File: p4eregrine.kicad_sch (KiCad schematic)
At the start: 45 parts, among them U1 ESP32-P4NRW32X, U15 TPD2EUSB30A, U3 W25Q128JVP, Y1 Crystal_GND24

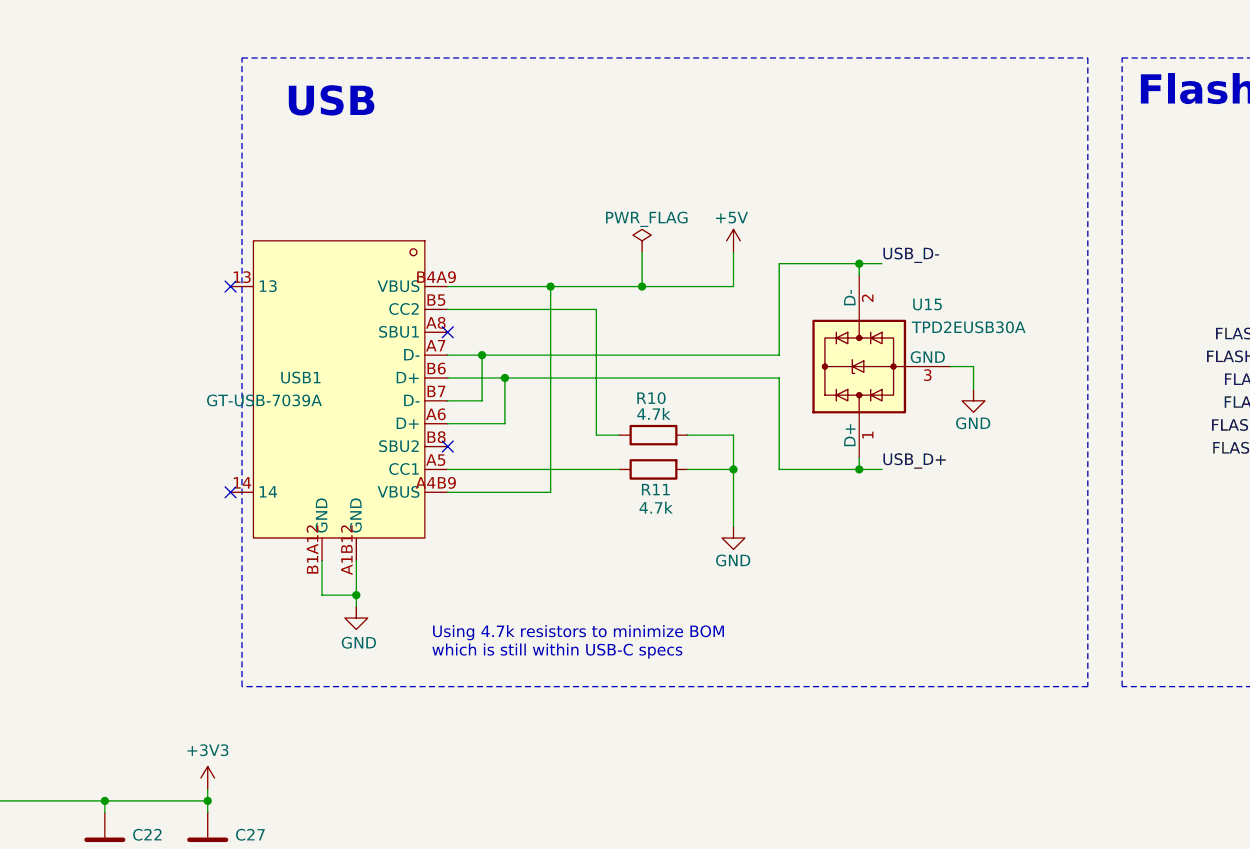
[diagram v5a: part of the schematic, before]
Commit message: Fix some silkscreen overlapping copper issues
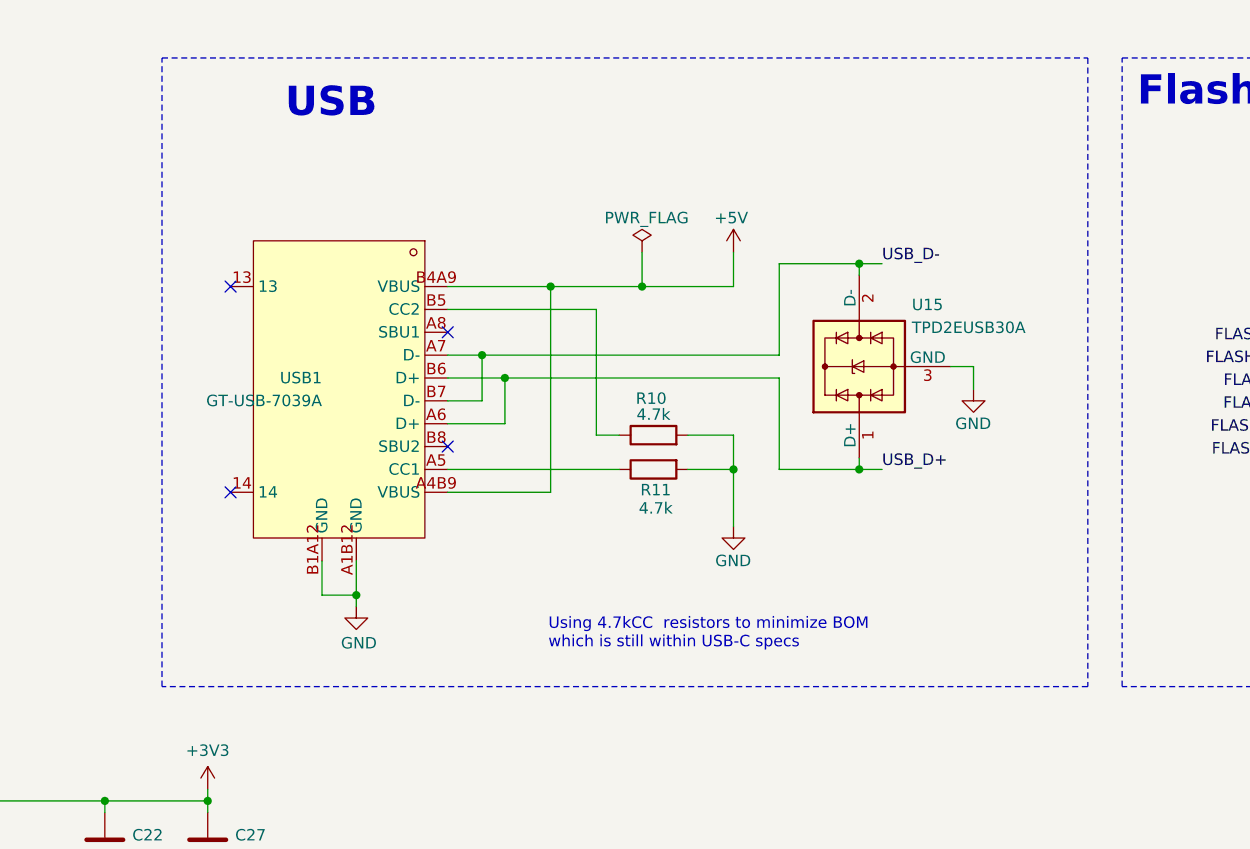
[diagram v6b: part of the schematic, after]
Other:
- note added: "Using 4.7kCC resistors to minimize BOM which is still within USB-C specs"
- note removed: "Using 4.7k resistors to minimize BOM which is still within USB-C specs"
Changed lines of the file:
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@@
 	)
 	(rectangle
-		(start 240.03 19.05)
+		(start 231.14 19.05)
 		(end 334.01 88.9)
 		(stroke
@@
 		)
 	)
-	(text "Using 4.7k resistors to minimize BOM\nwhich is still within USB-C specs"
+	(text "Using 4.7kCC  resistors to minimize BOM\nwhich is still within USB-C specs"
 		(exclude_from_sim no)
-		(at 261.112 84.074 0)
+		(at 274.066 83.058 0)
 		(effects
 			(font

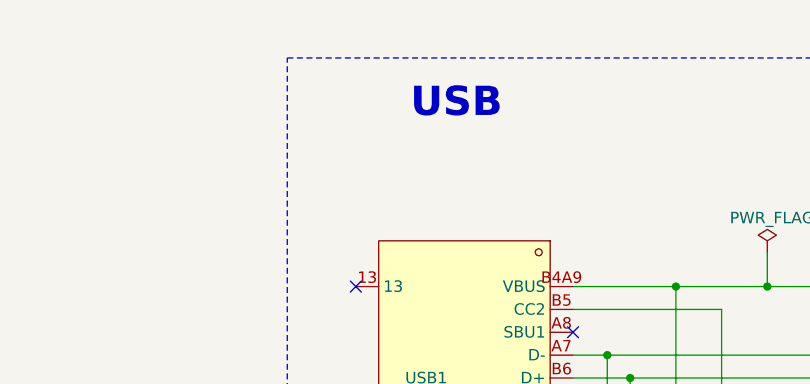
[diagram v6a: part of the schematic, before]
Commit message: Make GND probe pads square
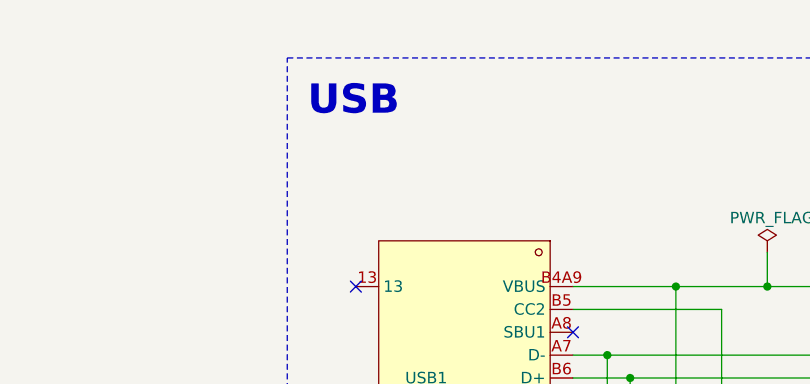
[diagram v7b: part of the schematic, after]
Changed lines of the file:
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@@
 	(text "USB"
 		(exclude_from_sim no)
-		(at 249.936 24.13 0)
+		(at 238.506 23.876 0)
 		(effects
 			(font

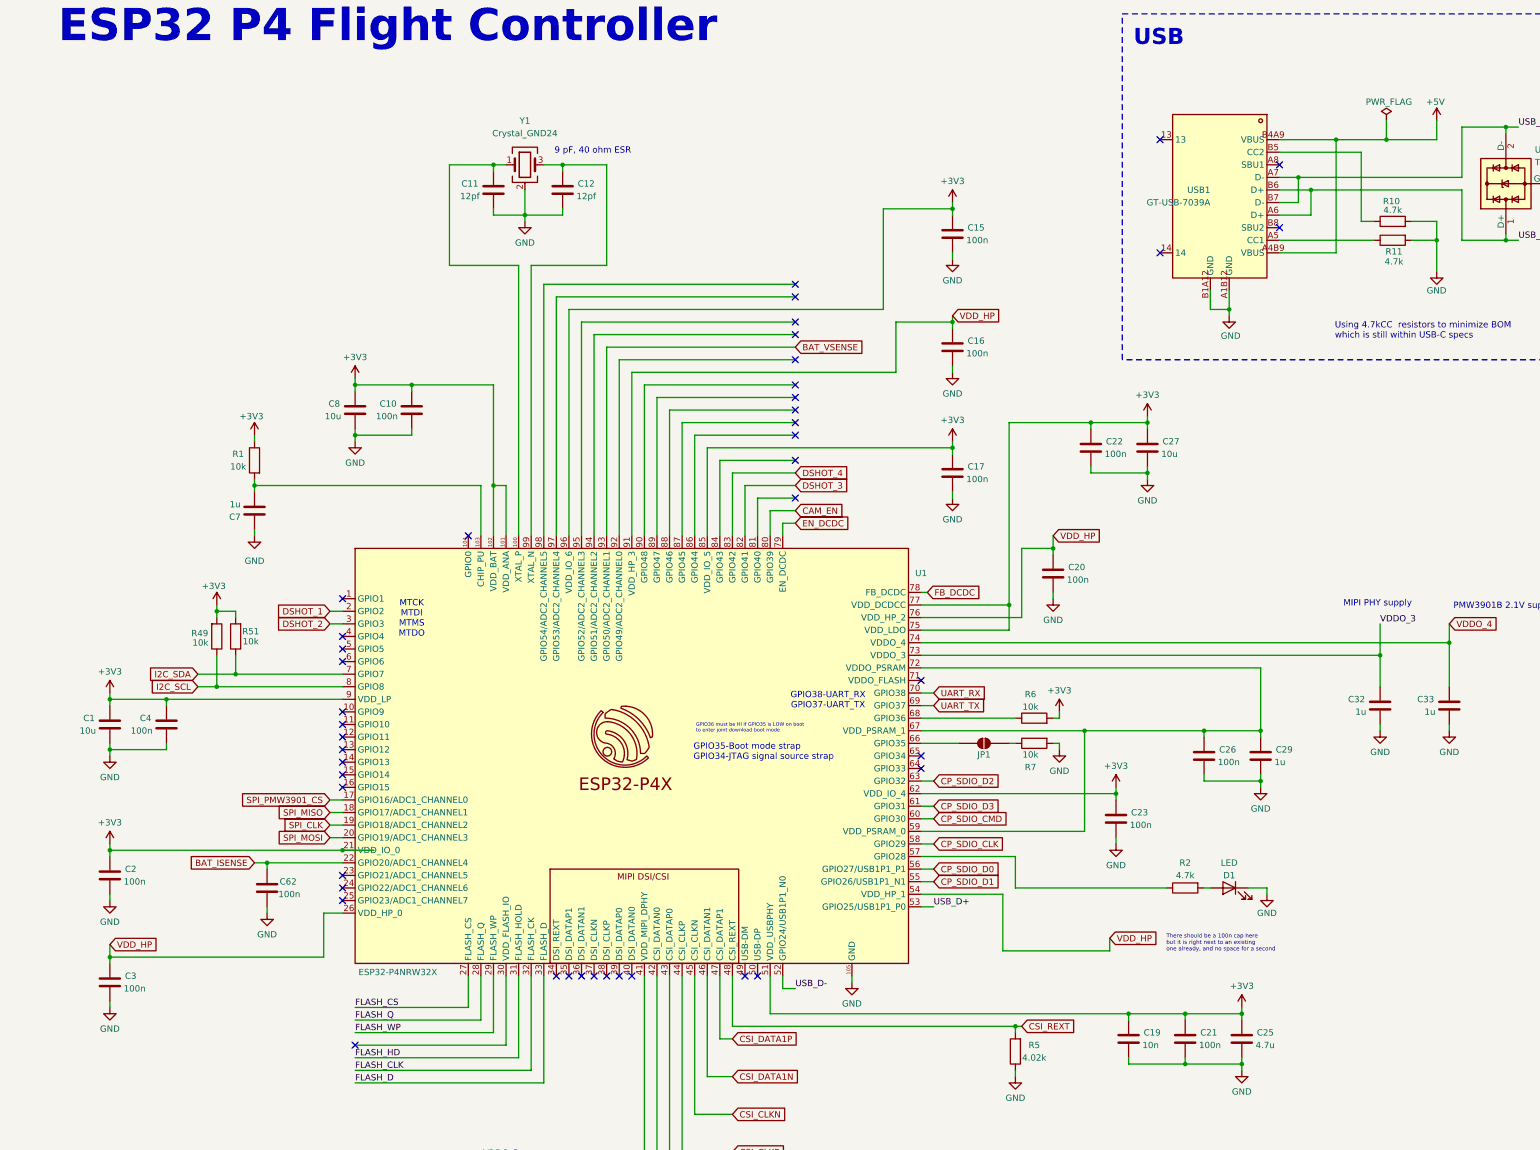
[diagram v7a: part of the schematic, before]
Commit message: Rename VBUS->VMUX, 5V->VBUS
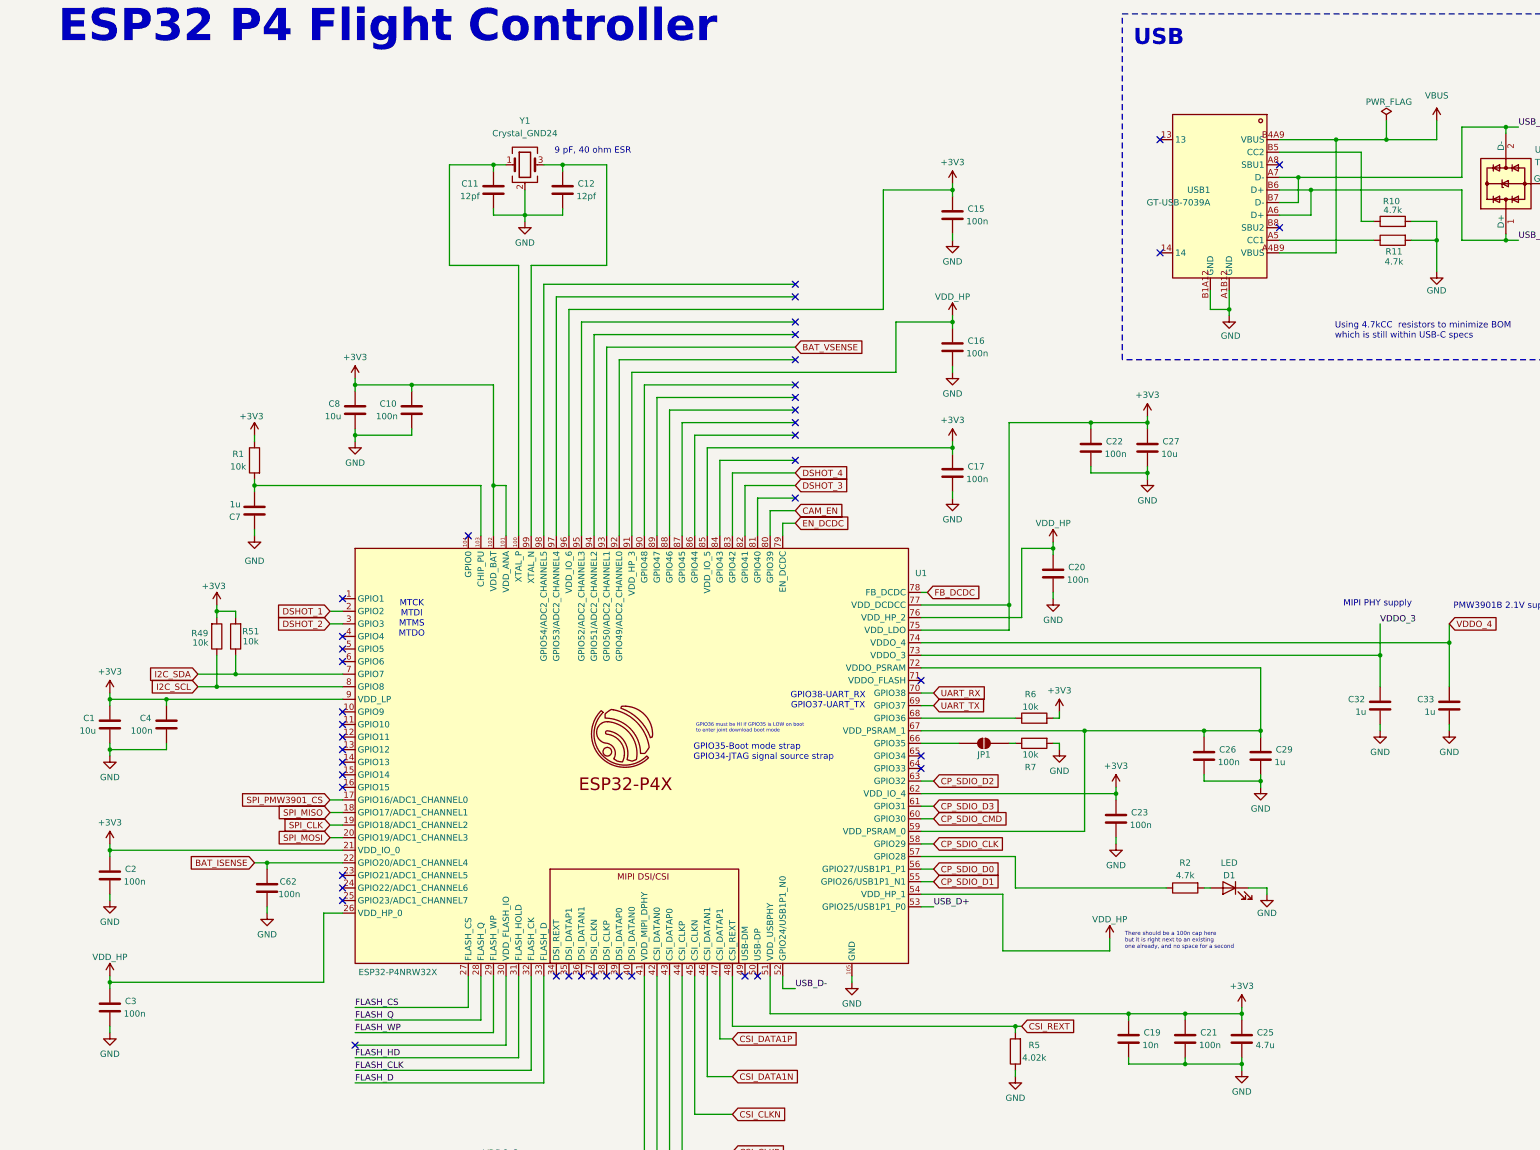
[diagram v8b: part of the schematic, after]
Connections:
- net +5V renamed VBUS
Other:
- moved on the sheet: C15, C3
